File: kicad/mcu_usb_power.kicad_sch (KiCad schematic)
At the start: 44 parts, among them J2 USB4105-GF-A, U7 MCXN947VDFT, U8 PCMF1USB3SZ

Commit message: Updated PCB layout
Updated all vias to have an annular ring always on the top and bottom layer. This was needed for Vekatech for production.
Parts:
- C55: DigiKey (none) -> 490-14440-1-ND; JLCPCB C77083 -> C161281; MFPN GRM21BR71H105KA12L -> GJ821BR71H105KA12L
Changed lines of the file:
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@@
 			)
 		)
-		(property "MFPN" "GRM21BR71H105KA12L"
+		(property "MFPN" "GJ821BR71H105KA12L"
 			(at 96.52 196.85 0)
 			(effects
@@
 			)
 		)
-		(property "JLCPCB" "C77083"
+		(property "JLCPCB" "C161281"
 			(at 96.52 196.85 0)
 			(effects
+				(font
+					(size 1.27 1.27)
+				)
+				(hide yes)
+			)
+		)
+		(property "DigiKey" "490-14440-1-ND"
+			(at 96.52 196.85 0)
+			(effects

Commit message: Update repo naming and cleanup files.
Signed-off-by: Benjamin Perseghetti <bperseghetti@rudislabs.com>
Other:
- title: MR-MCXN-T1 Sensor Node -> MR-MCXN-T1

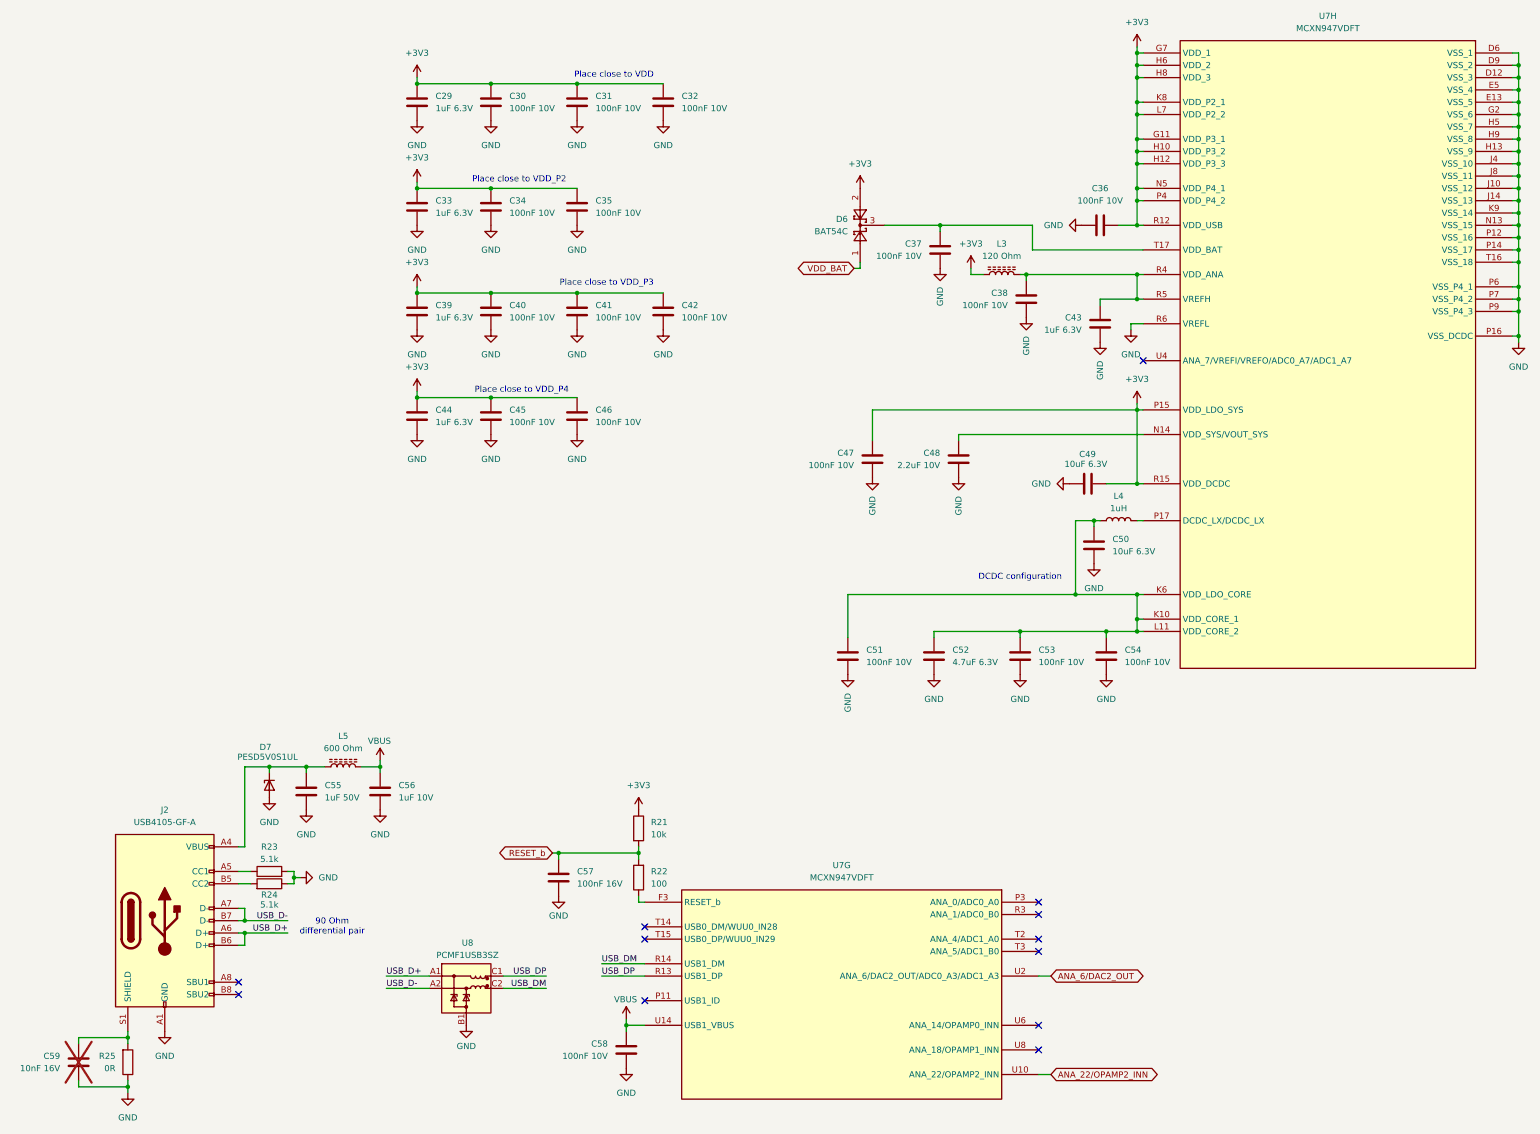
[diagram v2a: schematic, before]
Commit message: Patched schematic and board layout
- Replaced choke in series with Vbus with 2A choke.
- Fixed interface to the BMP581 barometer.
- Added schematic fixes to the layout.
- Completed DRC.
- Created production folder with Gerber, BOM, positions and schematic.
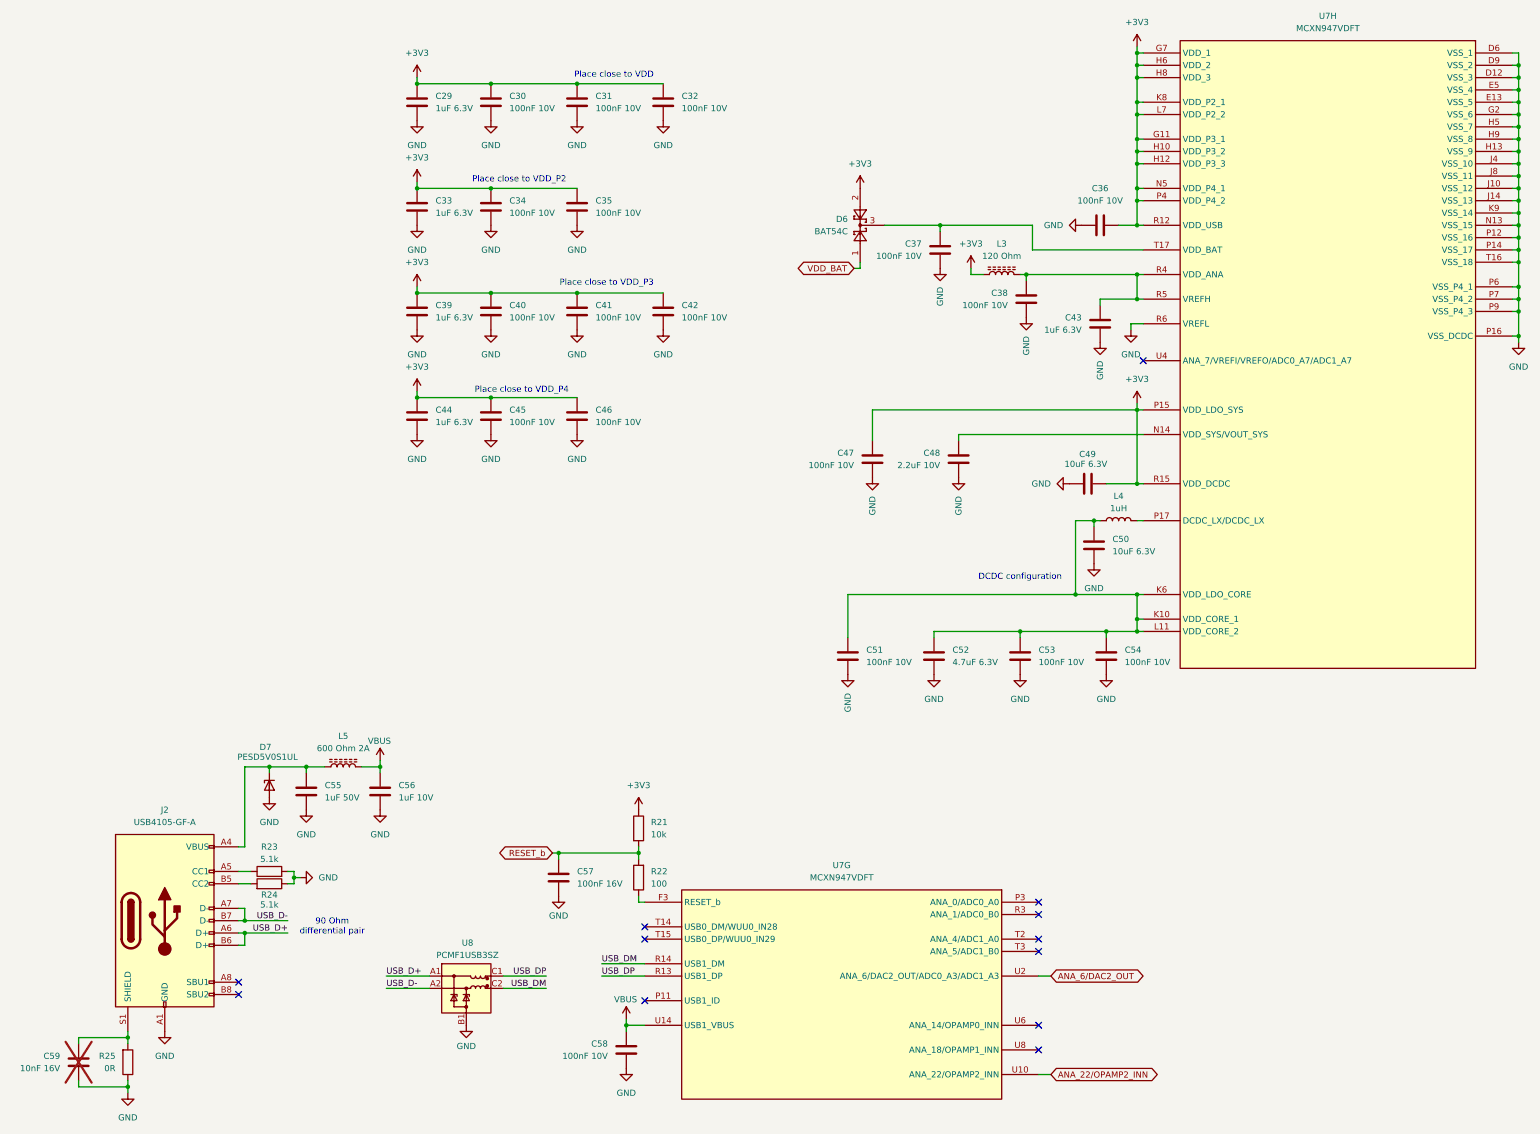
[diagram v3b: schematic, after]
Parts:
- C59: DigiKey (none) -> 490-4516-1-ND
- L5: value 600 Ohm -> 600 Ohm 2A; footprint Inductor_SMD:L_0402_1005Metric -> Inductor_SMD:L_0805_2012Metric; DigiKey 490-1006-1-ND -> 445-MPZ2012S601ATD25CT-ND; JLCPCB C76884 -> (none); MF Murata Electronics -> TDK Corporation; MFPN BLM15AG601SN1D -> MPZ2012S601ATD25
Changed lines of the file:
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@@
 (kicad_sch
-	(version 20231120)
+	(version 20250114)
 	(generator "eeschema")
-	(generator_version "8.0")
+	(generator_version "9.0")
 	(paper "A3")
 	(title_block
@@
 		(comment 4 "CTO SYSTEM INNOVATIONS / MOBILE ROBOTICS DOMAIN")
 	)
+	(text "Place close to VDD"
+		(exclude_from_sim no)
+		(at 160.02 49.022 0)
+		(effects
+			(font
+				(size 1.27 1.27)
+			)
+		)
+	)
+	(text "Place close to VDD_P4"
+		(exclude_from_sim no)
+		(at 140.97 114.046 0)
+		(effects
+			(font
+				(size 1.27 1.27)
+			)
+		)
+	)
+	(text "90 Ohm \ndifferential pair"
+		(exclude_from_sim no)
+		(at 101.854 224.79 0)
+		(effects
+			(font
+				(size 1.27 1.27)
+			)
+		)
+	)
+	(text "DCDC configuration"
+		(exclude_from_sim no)
+		(at 243.84 152.654 0)
+		(effects
+			(font
+				(size 1.27 1.27)
+			)
+		)
+	)
+	(text "Place close to VDD_P3"
+		(exclude_from_sim no)
+		(at 158.496 91.948 0)
+		(effects
+			(font
+				(size 1.27 1.27)
+			)
+		)
+	)
+	(text "Place close to VDD_P2"
+		(exclude_from_sim no)
+		(at 140.462 70.612 0)
+		(effects
+			(font
+				(size 1.27 1.27)
+			)
+		)
+	)
 	(junction
 		(at 346.71 97.79)
@@
 		)
 	)
-	(text "Place close to VDD"
-		(exclude_from_sim no)
-		(at 160.02 49.022 0)
-		(effects
-			(font
-				(size 1.27 1.27)
-			)
-		)
-	)
-	(text "Place close to VDD_P4"
-		(exclude_from_sim no)
-		(at 140.97 114.046 0)
-		(effects
-			(font
-				(size 1.27 1.27)
-			)
-		)
-	)
-	(text "90 Ohm \ndifferential pair"
-		(exclude_from_sim no)
-		(at 101.854 224.79 0)
-		(effects
-			(font
-				(size 1.27 1.27)
-			)
-		)
-	)
-	(text "DCDC configuration"
-		(exclude_from_sim no)
-		(at 243.84 152.654 0)
-		(effects
-			(font
-				(size 1.27 1.27)
-			)
-		)
-	)
-	(text "Place close to VDD_P3"
-		(exclude_from_sim no)
-		(at 158.496 91.948 0)
-		(effects
-			(font
-				(size 1.27 1.27)
-			)
-		)
-	)
-	(text "Place close to VDD_P2"
-		(exclude_from_sim no)
-		(at 140.462 70.612 0)
-		(effects
-			(font
-				(size 1.27 1.27)
-			)
-		)
-	)
 	(label "USB_D+"
 		(at 113.03 234.95 0)
@@
 			)
 		)
-		(property "Value" "600 Ohm"
+		(property "Value" "600 Ohm 2A"
 			(at 104.14 187.96 90)
 			(effects
@@
 			)
 		)
-		(property "Footprint" "Inductor_SMD:L_0402_1005Metric"
+		(property "Footprint" "Inductor_SMD:L_0805_2012Metric"
 			(at 104.14 191.77 0)
 			(effects
@@
 			)
 		)
-		(property "Datasheet" "https://www.murata.com/en-us/products/productdata/8796740059166/ENFA0018.pdf"
+		(property "Datasheet" "https://product.tdk.com/en/system/files/dam/doc/product/emc/emc/beads/catalog/beads_automotive_power_mpz2012_en.pdf"
 			(at 104.14 191.77 0)
 			(effects
@@
 			)
 		)
-		(property "Description" "600 Ohms @ 100 MHz 1 Ferrite Bead 0402 (1005 Metric) 300mA 520mOhm"
+		(property "Description" "600 Ohms @ 100 MHz 1 Power Line Ferrite Bead 0805 (2012 Metric) 2A 100mOhm"
 			(at 104.14 191.77 0)
 			(effects
@@
 			)
 		)
-		(property "MF" "Murata Electronics"
+		(property "MF" "TDK Corporation"
 			(at 104.14 191.77 0)
 			(effects
@@
 			)
 		)
-		(property "MFPN" "BLM15AG601SN1D"
+		(property "MFPN" "MPZ2012S601ATD25"
 			(at 104.14 191.77 0)
 			(effects
@@
 			)
 		)
-		(property "JLCPCB" "C76884"
-			(at 104.14 191.77 0)
-			(effects
-				(font
-					(size 1.27 1.27)
-				)
-				(hide yes)
-			)
-		)
-		(property "DigiKey" "490-1006-1-ND "
+		(property "DigiKey" "445-MPZ2012S601ATD25CT-ND"
 			(at 104.14 191.77 0)
 			(effects
@@
 			(at 49.53 252.73 0)
 			(effects
+				(font
+					(size 1.27 1.27)
+				)
+				(hide yes)
+			)
+		)
+		(property "DigiKey" "490-4516-1-ND"
+			(at 49.53 252.73 0)
+			(effects
